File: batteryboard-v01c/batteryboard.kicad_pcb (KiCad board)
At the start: 4 copper layers, 95.9 x 90.2 mm, 83 parts, among them J1 KEYSTONE-1042, J2 KEYSTONE-1042, J3 KEYSTONE-1042, J4 KEYSTONE-1042, J5 KEYSTONE-1042, J6 KEYSTONE-1042, J7 Molex 5023521200, J8 Screw_Terminal_01x02, J9 Molex 5023520600, Q1 IRF7458, Q10 IRLML2803, Q11 IRF7404TRPBF, Q2 IRF7458, Q3 IRLML2803, Q4 CSD17579Q5A, Q5 CSD17579Q5A, Q6 BSS138DWQ-7, Q7 MBT2222ADW1T1, Q8 BSS138DWQ-7, Q9 MBT2222ADW1T1, U1 R5460N233AF, U2 BQ28Z620

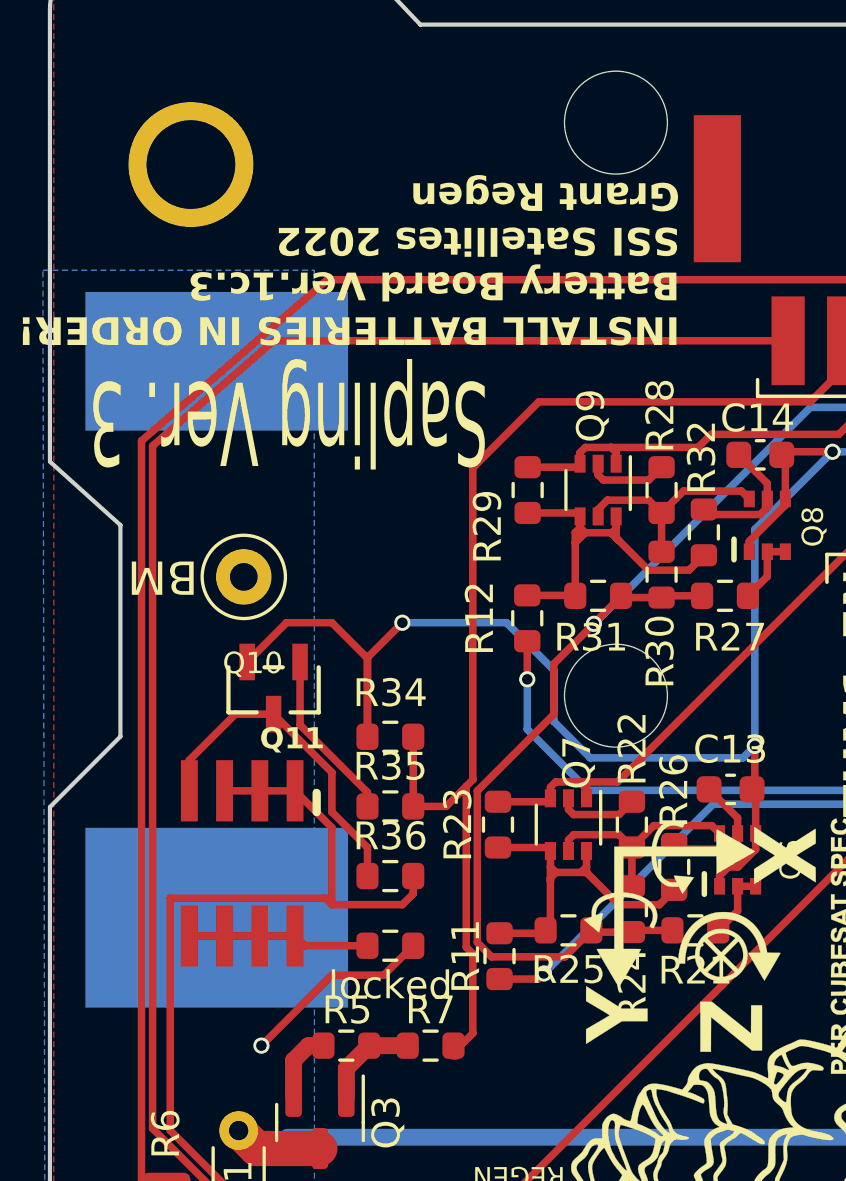
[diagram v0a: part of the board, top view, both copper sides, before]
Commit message: updated silkscreen
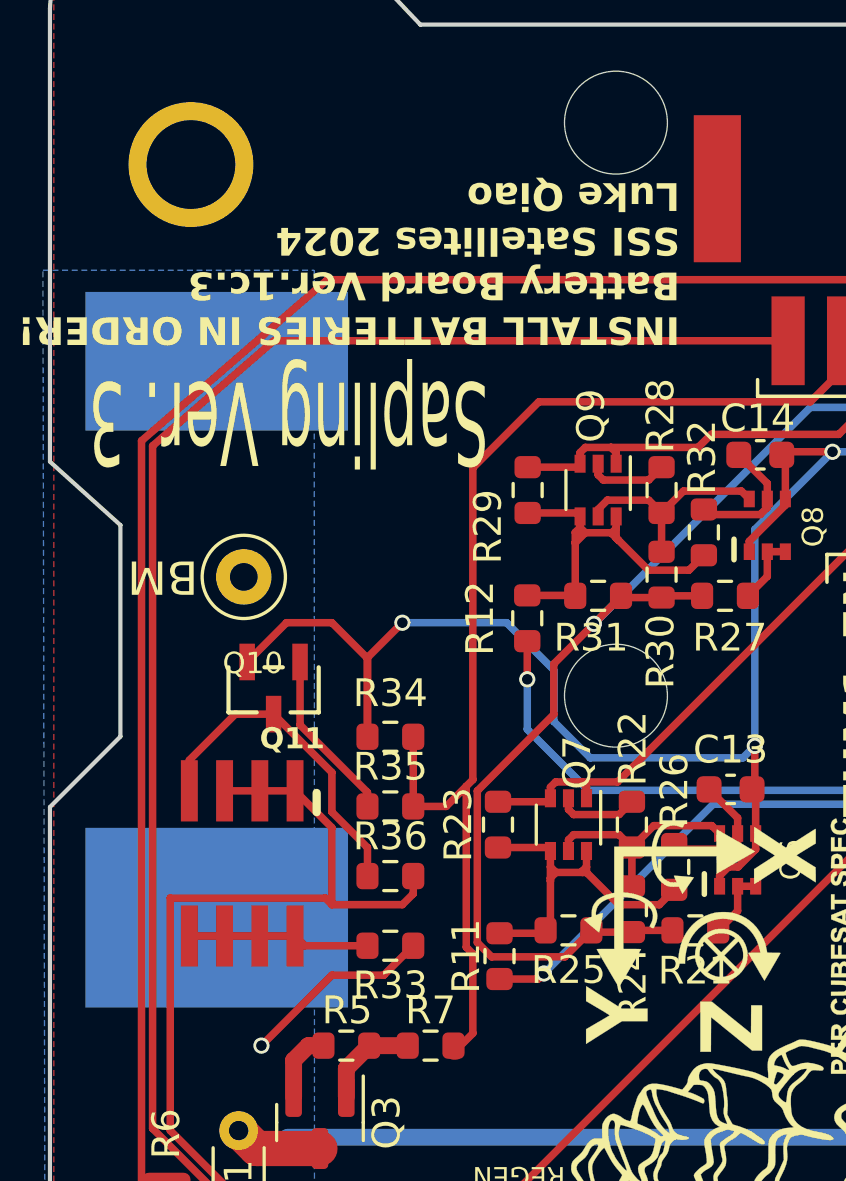
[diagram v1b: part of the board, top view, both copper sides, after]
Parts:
- renumbered locked to R33
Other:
- board text added: "INSTALL BATTERIES IN ORDER! Battery Board Ver.1c.3 SSI Satellites 2024 Luke Qiao"
- board text removed: "INSTALL BATTERIES IN ORDER! Battery Board Ver.1c.3 SSI Satellites 2022 Grant Regen"
